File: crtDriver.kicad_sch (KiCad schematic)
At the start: 23 parts, among them J1 Lum_In, J2 V_Sync, J4 H_Sync, Q1 2N7000, Q2 2N7000, Q3 2N7000, Q4 2N7000, Q5 2N7000

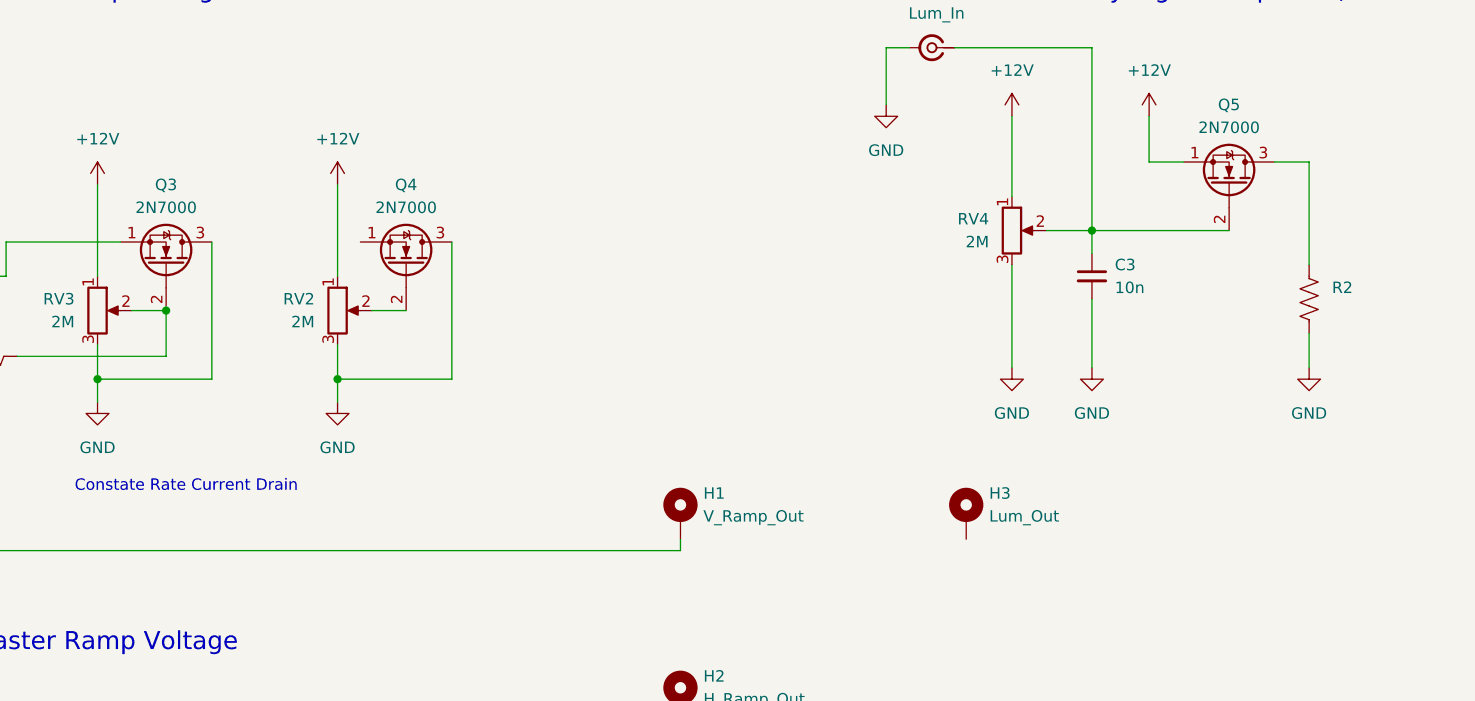
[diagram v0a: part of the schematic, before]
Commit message: got potentiometer parameters to show in ui, got spice simulation to run
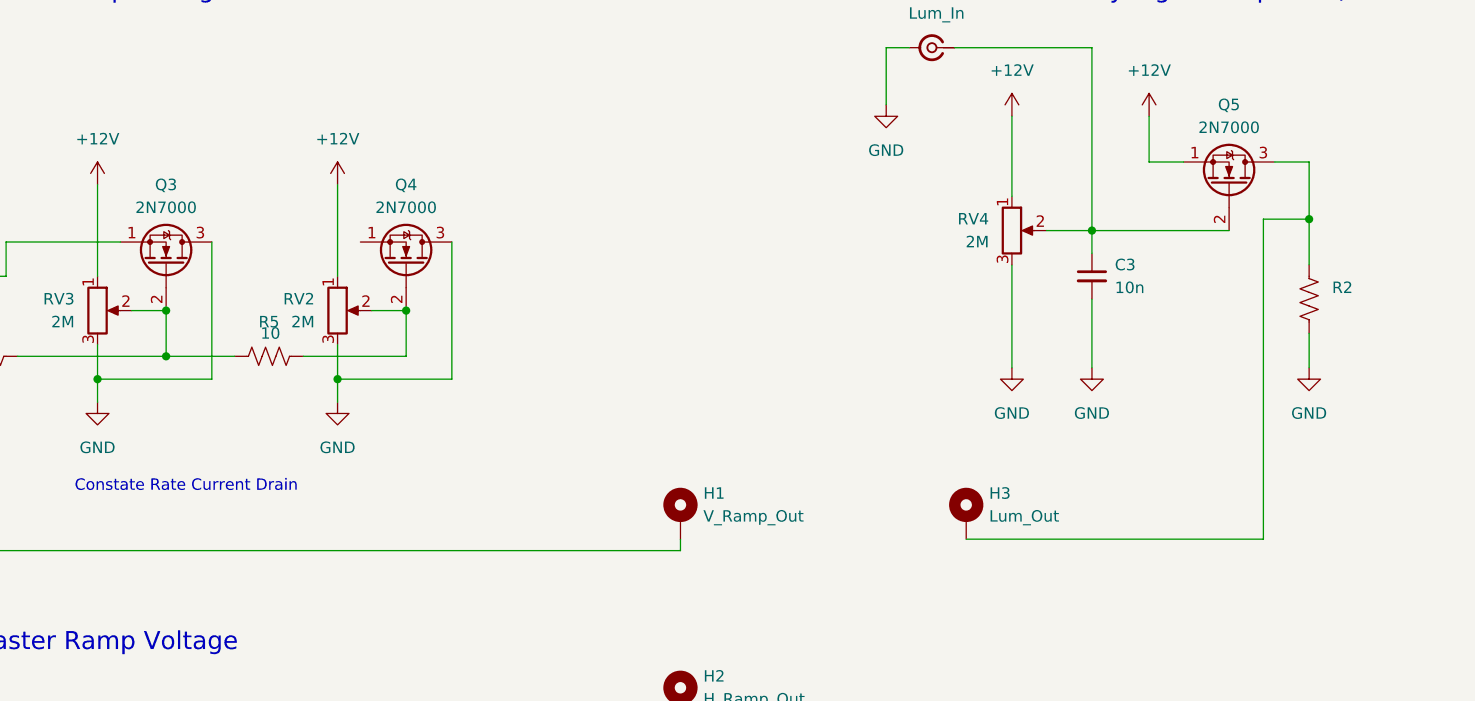
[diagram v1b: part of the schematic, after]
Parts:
- added R5: 10, symbol Device:R_US
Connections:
- net at Q4.2 (G), RV2.2: now also R5.2
- net at Q3.2 (G), R3.2, RV3.2: now also R5.1
- net at Q5.3 (D), R2.1: now also H3.1

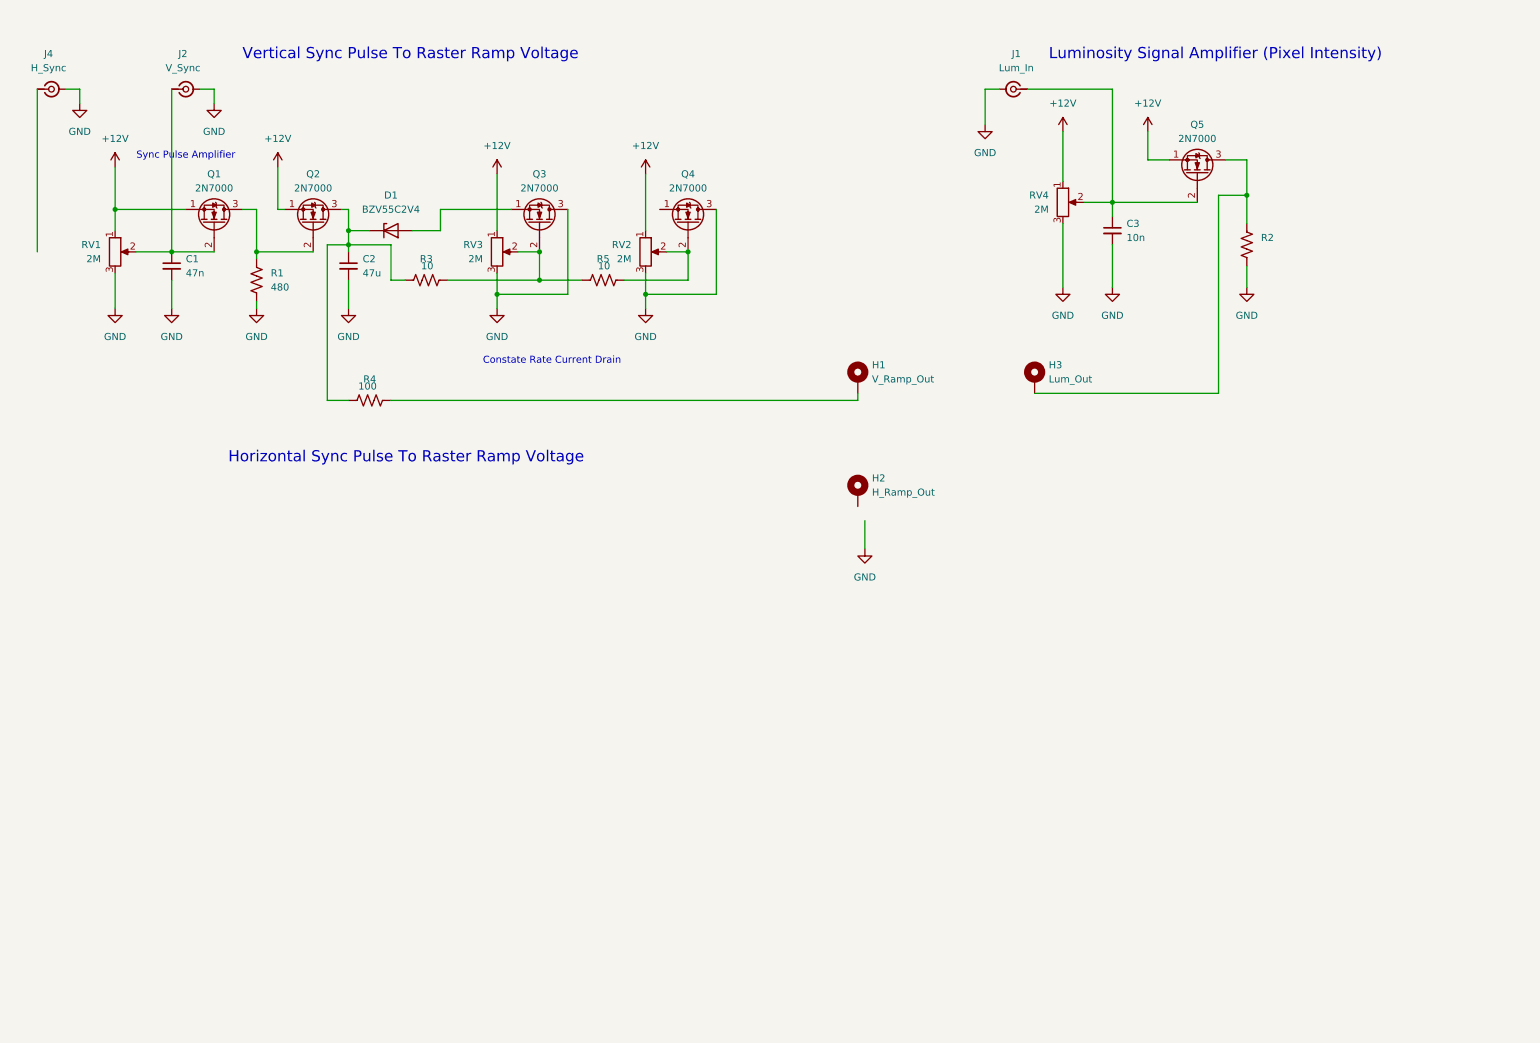
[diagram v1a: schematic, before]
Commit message: got spice simulation to run with +V, v sync input. added 2n7000 model and fixed potentiometer model pinout
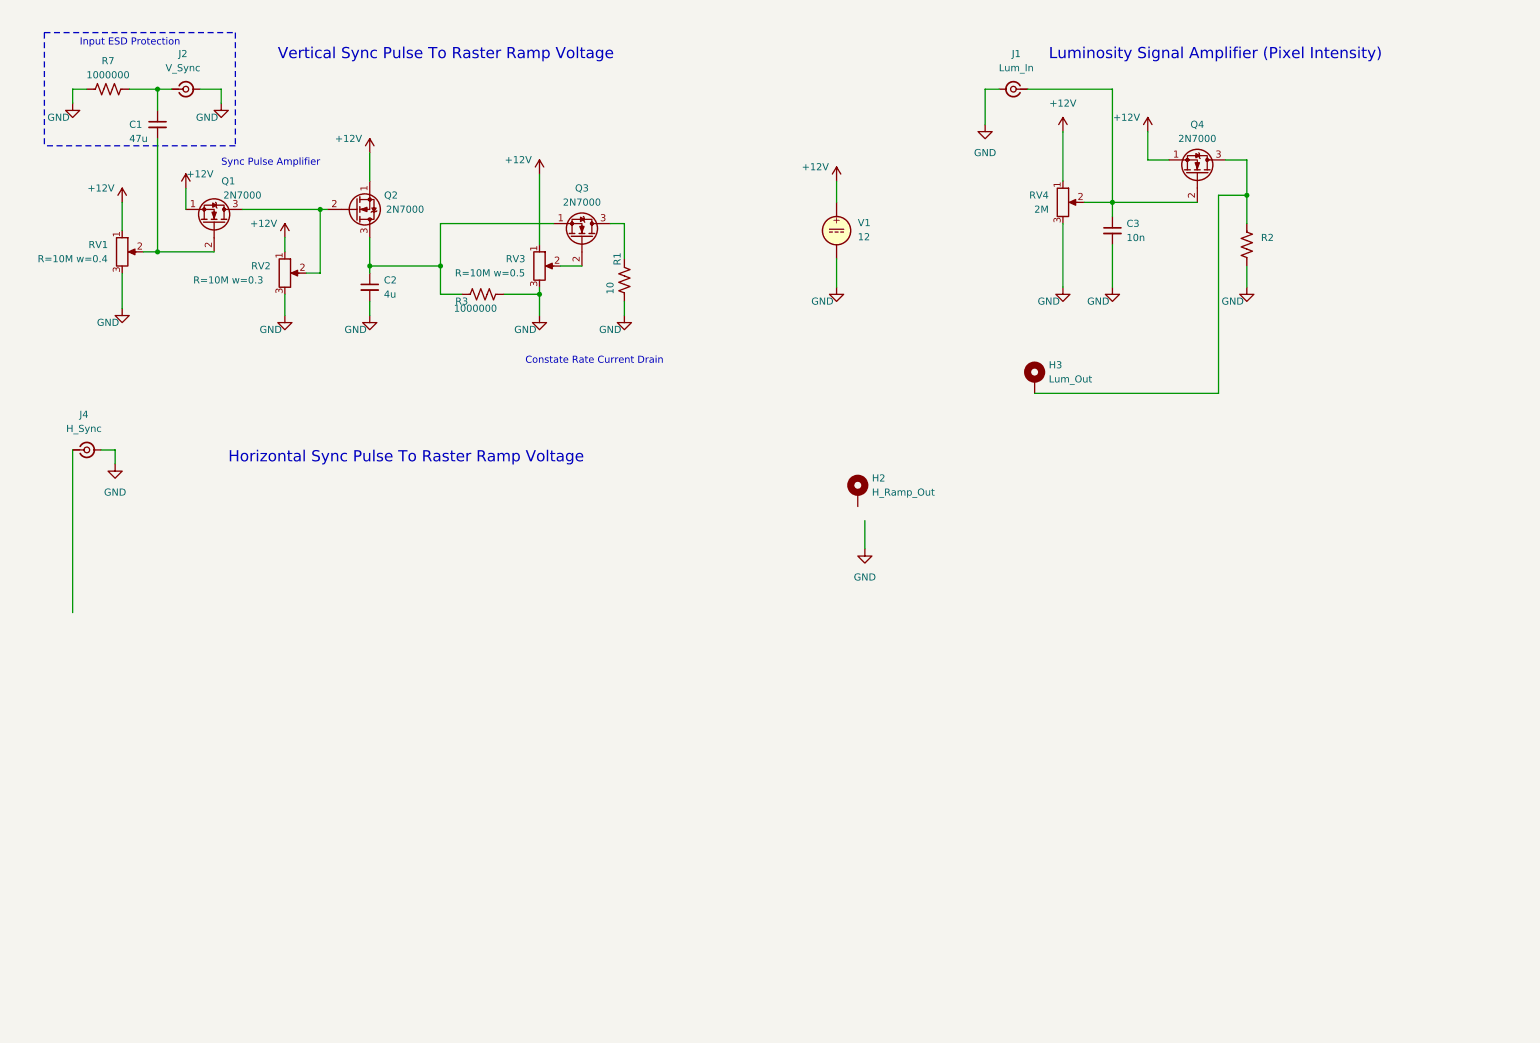
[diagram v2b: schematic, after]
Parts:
- removed D1: BZV55C2V4, Diode_SMD:D_MiniMELF, symbol Diode:BZV55C2V4
- removed H1: V_Ramp_Out, symbol Mechanical:MountingHole_Pad
- removed Q5: 2N7000, Package_TO_SOT_THT:TO-92_Inline, symbol Transistor_FET:2N7000
- removed R4: 100, symbol Device:R_US
- removed R5: 10, symbol Device:R_US
- added R7: 1000000, symbol Device:R_US
- added V1: 12, symbol Simulation_SPICE:VDC
- C1: value 47n -> 47u
- C2: value 47u -> 4u
- R1: value 480 -> 10
- R3: value 10 -> 1000000
- RV3: value 2M -> 10M
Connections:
- net +12V: now also Q4.1 (S), V1.1
- net GND: now also R3.2, R7.2, V1.2; no longer C1.2, Q3.3 (D), Q4.3 (D)
- net at Q4.2 (G): now also C3.1, J1.1 (In), RV4.2; no longer RV2.2
- net at C2.1, Q2.3 (D), R3.1: now also Q3.1 (S)
- net at Q3.2 (G), RV3.2: no longer R3.2
- net at Q1.3 (D), Q2.2 (G): now also RV2.2; no longer R1.1
- net at C1.1, J2.1 (In): now also R7.1; no longer Q1.2 (G), RV1.2
- net at H3.1, R2.1: now also Q4.3 (D)
- new net: C1.2, Q1.2 (G), RV1.2
- new net: Q3.3 (D), R1.1
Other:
- note added: "Input ESD Protection"
- moved on the sheet: C2, J4, R3, RV1, RV3

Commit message: added 3d model for potentiometer, started on component placement and trace routing
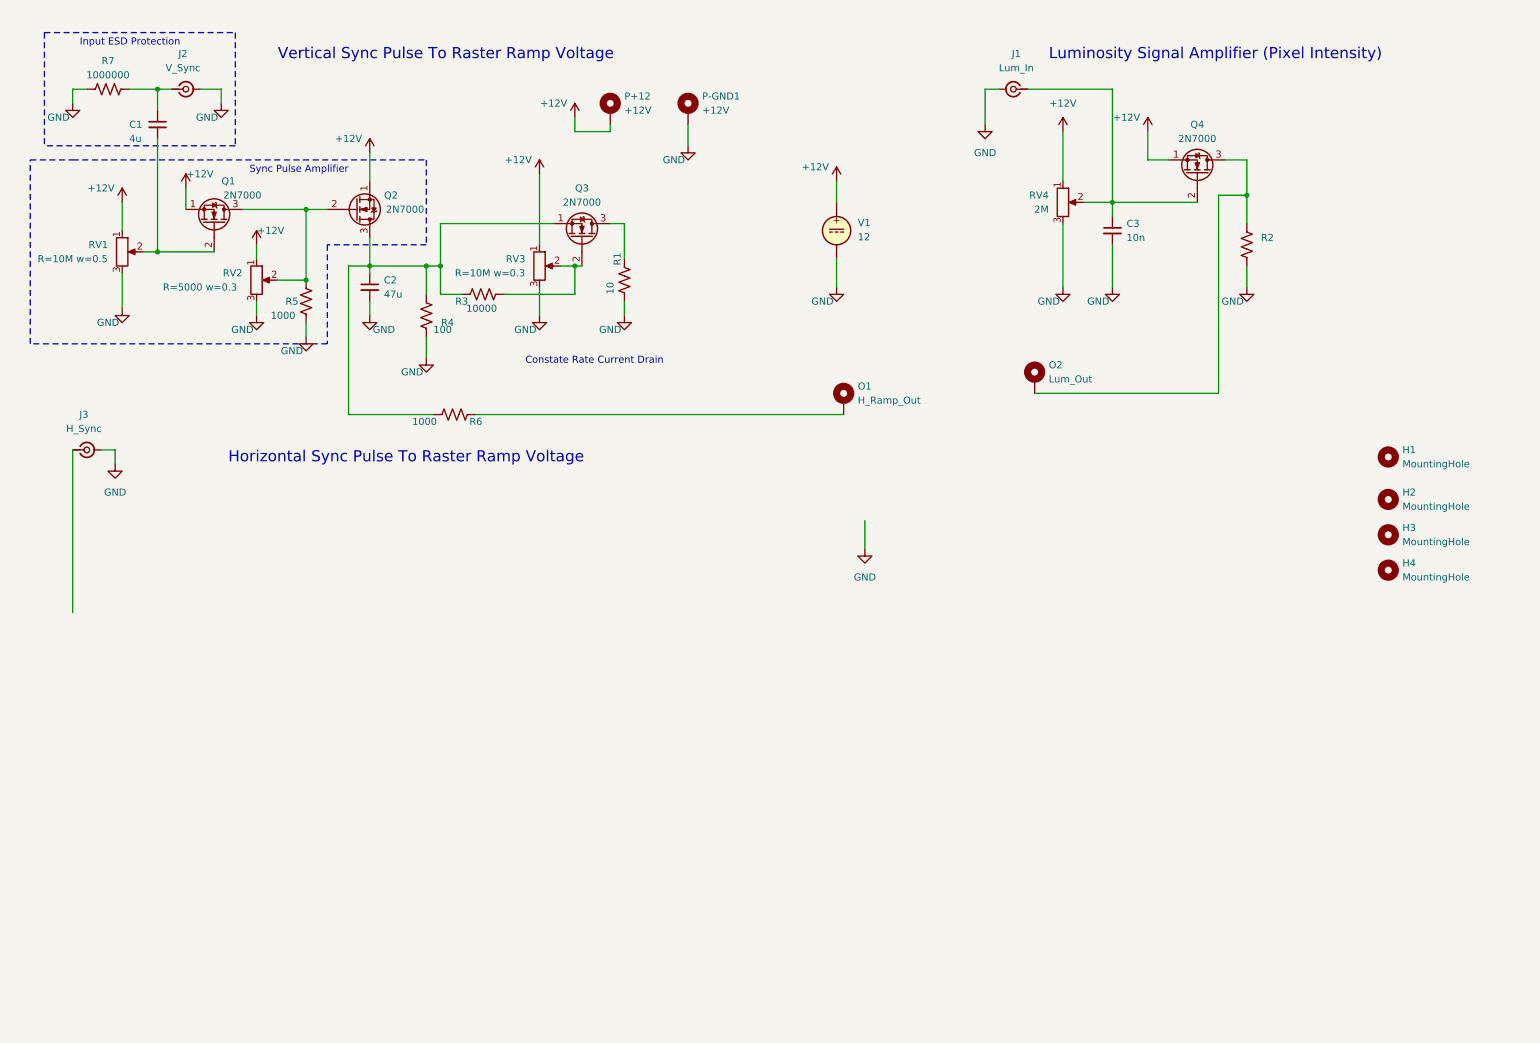
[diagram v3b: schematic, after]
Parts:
- added H1, H2, H3, H4: MountingHole, MountingHole:MountingHole_2.5mm, symbol Mechanical:MountingHole
- added P+12, P-GND1: +12V, Connector_Wire:SolderWire-0.25sqmm_1x01_D0.65mm_OD2mm_Relief, symbol Mechanical:MountingHole_Pad
- added R4: 100, Resistor_SMD:R_1210_3225Metric, symbol Device:R_US
- added R5: 1000, Resistor_SMD:R_0805_2012Metric, symbol Device:R_US
- added R6: 1000, Resistor_SMD:R_0603_1608Metric, symbol Device:R_US
- C1: value 47u -> 4u; footprint (none) -> Capacitor_SMD:C_0603_1608Metric
- C2: value 4u -> 47u; footprint (none) -> Capacitor_SMD:C_1206_3216Metric
- C3: footprint (none) -> Capacitor_SMD:C_0603_1608Metric
- J1, J2: footprint (none) -> Connector_Coaxial:SMA_Amphenol_901-144_Vertical
- J3: renamed from J4; footprint (none) -> Connector_Coaxial:SMA_Amphenol_901-144_Vertical
- O1: renamed from H2; footprint (none) -> Connector_Wire:SolderWire-0.25sqmm_1x01_D0.65mm_OD2mm_Relief
- O2: renamed from H3; footprint (none) -> Connector_Wire:SolderWire-0.25sqmm_1x01_D0.65mm_OD2mm_Relief
- R1: footprint (none) -> Resistor_SMD:R_1210_3225Metric
- R2: footprint (none) -> Resistor_SMD:R_0805_2012Metric
- R3: value 1000000 -> 10000; footprint (none) -> Resistor_SMD:R_0603_1608Metric
- R7: footprint (none) -> Resistor_SMD:R_0603_1608Metric
- RV1, RV2, RV3, RV4: footprint (none) -> crtDriver:Potentiometer_Triwood_RM-065
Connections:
- net +12V: now also P+12.1
- net GND: now also P-GND1.1, R4.2, R5.2; no longer R3.2
- net at O1.1: now also R6.1
- net at C2.1, Q2.3 (D), Q3.1 (S)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: now also R4.1, R6.2
- net at Q1.3 (D), Q2.2 (G), RV2.2: now also R5.1
- net at Q3.2 (G), RV3.2: now also R3.2
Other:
- moved on the sheet: O1, RV2
